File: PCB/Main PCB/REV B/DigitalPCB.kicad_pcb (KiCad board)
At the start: 4 copper layers, 60 x 80 mm, 102 parts, among them J1 DF12NC-20DS-0.5V_51_, J2 1050170001, J3 Hopper, J4 Screen, J5 Spare1, J6 Spare2, Q1 MBT3904DW1, U1 AMS1117-3.3, U2 ESP32-WROOM-32UE_16MB, U3 TPS2115APWR, U4 TLP2362TPR_E, U5 CP2102N-A02-GQFN24, U6 TLP2362TPR_E, U7 TLP2362TPR_E, U8 STM811SW16F

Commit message: PCB - digital routing underway
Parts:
- moved C12 1.10 mm to (101.8, 109.0)
- moved D2 1.10 mm to (98.0, 109.0)
- moved D6 1.10 mm to (100.8, 105.7)
- moved R2 1.10 mm to (99.9, 109.0)
- moved R27 0.30 mm to (95.9, 107.7)
- turned C1 to 0 degrees
- turned C7 to 90 degrees
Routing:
- net +3.3VA: track 0.00 -> 81.9 mm, vias 0 -> 9
- net +5VA: track 0.00 -> 20.3 mm
- net /IO13: track 0.00 -> 13.6 mm
- net /IO27: track 0.00 -> 13.2 mm
- net /IO26: track 0.00 -> 13.0 mm
- net /IO25: track 0.00 -> 12.8 mm
- net GND: track 0.00 -> 8.65 mm, vias 0 -> 52
- net +3.3V: track 0.00 -> 5.21 mm, vias 0 -> 19
- net Net-(JP1-Pad2): track 0.00 -> 4.62 mm
- net Net-(JP6-Pad2): track 0.00 -> 4.55 mm
- net Net-(JP2-Pad2): track 0.00 -> 4.26 mm
- net Net-(JP4-Pad2): track 0.00 -> 4.25 mm
- net Net-(D5-Pad2): track 0.00 -> 3.89 mm
- net Net-(D4-Pad2): track 0.00 -> 3.89 mm
- net Net-(D3-Pad2): track 0.00 -> 3.89 mm
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- added copper zone on F.Cu, net +3.3V
- added copper zone on In2.Cu, net +3.3V
- added copper zone on F.Cu, net +3.3VP
- added copper zone on B.Cu, net GND
- added copper zone on F.Cu, net GND
- added copper zone on In1.Cu, net GND

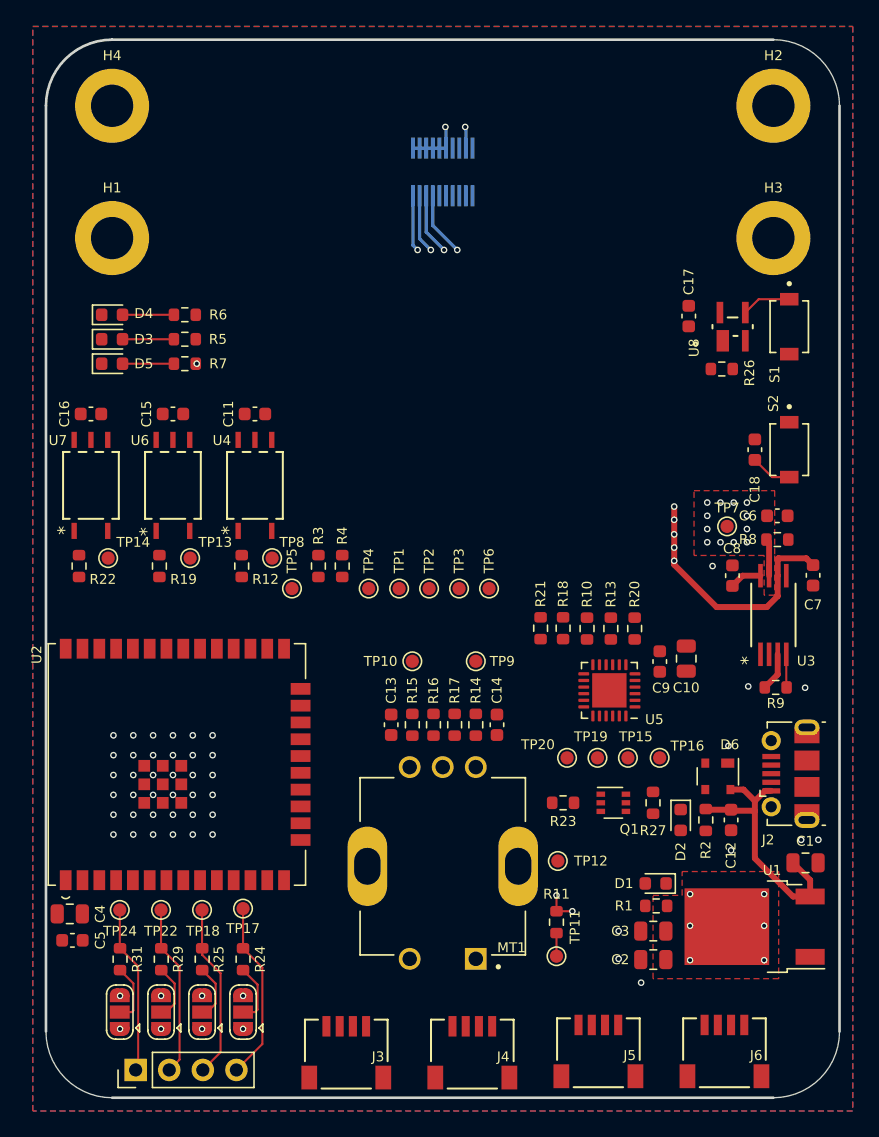
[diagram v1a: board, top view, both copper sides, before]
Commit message: PCB - digital routing halfway done
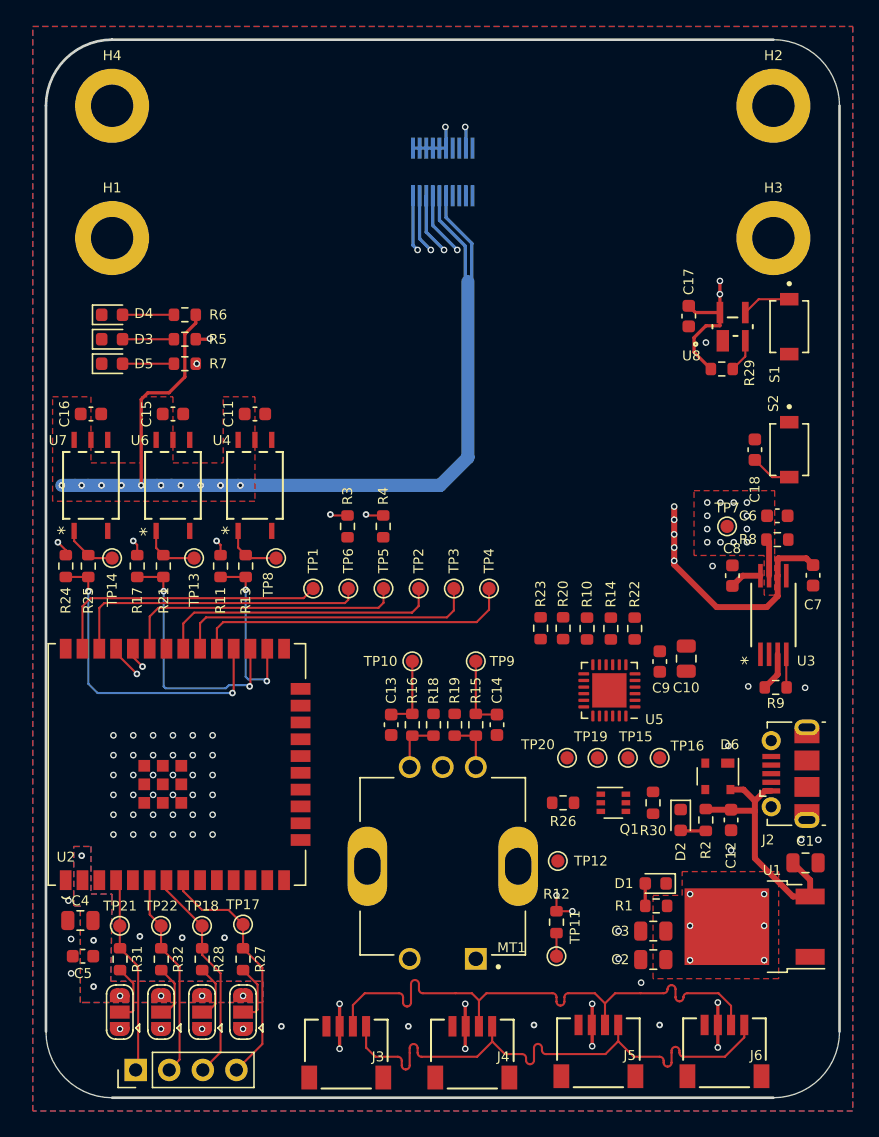
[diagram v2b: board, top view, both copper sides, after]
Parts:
- added R11: 10K 1% 0603, Resistor_SMD:R_0603_1608Metric, F.Cu at (63.2, 89.8)
- added R17: 10K 1% 0603, Resistor_SMD:R_0603_1608Metric, F.Cu at (56.9, 89.8)
- added R24: 10K 1% 0603, Resistor_SMD:R_0603_1608Metric, F.Cu at (51.5, 89.8)
- moved TP1 13.3 mm to (70.2, 91.5)
- moved R4 4.31 mm to (75.5, 86.8)
- moved TP6 4.26 mm to (72.9, 91.5)
- moved R3 3.72 mm to (72.8, 86.8)
- moved TP4 2.27 mm to (83.5, 91.5)
- moved TP3 1.87 mm to (80.8, 91.5)
- moved TP2 1.48 mm to (78.2, 91.5)
- moved C5 1.44 mm to (52.8, 119.3)
- moved TP17 1.20 mm to (64.9, 116.9)
- moved TP18 1.20 mm to (61.8, 117.0)
- moved TP21 1.20 mm to (55.6, 117.0)
- moved TP22 1.20 mm to (58.7, 117.0)
- moved TP5 1.12 mm to (75.5, 91.5)
- moved C4 0.94 mm to (52.6, 116.6)
- moved R25 0.70 mm to (53.2, 89.8)
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- renumbered JP6 to JP3, R11 to R12, R12 to R13, R13 to R14, R14 to R15, R15 to R16, R16 to R18, R17 to R19, R18 to R20, R19 to R21, R20 to R22, R21 to R23, R22 to R25, R23 to R26, R24 to R27, R25 to R28, R26 to R29, R27 to R30, R29 to R32, TP6 to TP1, TP1 to TP2, TP24 to TP21, TP26 to TP24, TP2 to TP3, TP3 to TP4, TP4 to TP5, TP5 to TP6
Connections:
- net /I39 renamed /IO39
- C13 pad 1: /IO32 -> /IO25
- C14 pad 1: /IO33 -> /IO26
- MT1 pad 2: /IO34 -> /IO33
- R12 pad 1: /IO34 -> /IO33
- R15 pad 2: /IO33 -> /IO26
- R16 pad 2: /IO32 -> /IO25
- R27 pad 1: /IO13 -> /IO32
- R28 pad 1: /IO27 -> /IO35
- R31 pad 1: /IO25 -> /IO36
- R32 pad 1: /IO26 -> /IO34
- TP10 pad 1: /IO32 -> /IO25
- TP11 pad 1: /IO34 -> /IO33
- TP17 pad 1: /IO13 -> /IO32
- TP18 pad 1: /IO27 -> /IO35
- TP21 pad 1: /IO25 -> /IO36
- TP22 pad 1: /IO26 -> /IO34
- TP24 pad 1: /IO25 -> /IO36
- TP24 pad 2: /IO26 -> /IO34
- TP24 pad 3: /IO27 -> /IO35
- TP24 pad 4: /IO13 -> /IO32
- TP9 pad 1: /IO33 -> /IO26
- U2 pad 23: /Auger -> /IO15
- U2 pad 26: /Fan -> /Auger
- U2 pad 27: /SPI_MOSI -> /Fan
- U2 pad 28: /IO17 -> /Ignitor
- U2 pad 37: /Ignitor -> /SPI_MOSI
- U2 pad 4: /I36 -> /IO36
- U2 pad 6: /I34 -> /IO34
- U2 pad 7: /I35 -> /IO35
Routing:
- net +5V: track 0.00 -> 75.2 mm, vias 0 -> 10
- net /I2C_SCL: track 0.00 -> 66.6 mm
- net /I2C_SDA: track 0.00 -> 64.8 mm
- net +3.3V: track 5.21 -> 36.1 mm, vias 19 -> 37
- net /Ignitor: track 0.00 -> 24.4 mm, vias 0 -> 2
- net /SPI_CS: track 0.00 -> 24.3 mm
- net /SPI_SCK: track 0.00 -> 23.2 mm
- net +3.3VA: track 81.9 -> 105.0 mm, vias 9 -> 10
- net /SPI_MISO: track 0.00 -> 21.6 mm
- net /SPI_MOSI: track 0.00 -> 21.2 mm
- net /Fan: track 0.00 -> 19.8 mm, vias 0 -> 2
- net /IO32: track 0.00 -> 18.8 mm
- net /TXD0: track 0.00 -> 17.3 mm, vias 0 -> 1
- net /IO35: track 0.00 -> 16.6 mm
- net /RXD0: track 0.00 -> 15.9 mm, vias 0 -> 1
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- added copper zone on B.Cu, net +3.3V
- added copper zone on F.Cu, net +5V

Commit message: PCB - digital routing first pass done
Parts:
- added C19: 0.1uF 50V X7R 0603, Capacitor_SMD:C_0603_1608Metric, F.Cu at (84.1, 78.0)
- added C20: 0.01uF 50V X7R 0603, Capacitor_SMD:C_0603_1608Metric, F.Cu at (86.8, 78.8)
- added U9: MAX31855KASA, Package_SO:SOIC-8_3.9x4.9mm_P1.27mm, F.Cu at (86.9, 83.6)
- moved TP16 7.31 mm to (94.0, 111.2)
- moved TP15 7.24 mm to (91.8, 111.2)
- moved R20 6.68 mm to (88.1, 101.1)
- moved R23 6.68 mm to (86.4, 101.1)
- moved TP20 4.63 mm to (88.9, 108.9)
- moved TP19 4.24 mm to (95.9, 104.9)
- moved D6 1.90 mm to (98.9, 105.7)
- moved R26 1.79 mm to (90.3, 106.4), turned to -90 degrees
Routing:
- net /EN: track 2.53 -> 96.3 mm, vias 0 -> 4
- net /MeatProbe-: track 0.00 -> 78.7 mm, vias 0 -> 1
- net /IO0: track 3.14 -> 80.3 mm, vias 0 -> 4
- net /MeatProbe+: track 0.00 -> 72.8 mm, vias 0 -> 1
- net /I2C_SDA: track 64.8 -> 120.1 mm, vias 0 -> 2
- net /I2C_SCL: track 66.6 -> 120.4 mm, vias 0 -> 2
- net /Opto_Fan: track 0.00 -> 51.9 mm, vias 0 -> 1
- net /Opto_Ignitor: track 0.00 -> 47.8 mm, vias 0 -> 1
- net +3.3VP: track 2.44 -> 38.6 mm, vias 6 -> 10
- net /Opto_Auger: track 0.00 -> 35.5 mm, vias 0 -> 1
- net +5V: track 75.2 -> 110.6 mm, vias 10 -> 14
- net /Probe1-: track 0.00 -> 32.9 mm, vias 0 -> 1
- net /IO33: track 1.75 -> 32.9 mm
- net /IO26: track 5.60 -> 35.3 mm
- net /IO25: track 5.60 -> 29.8 mm
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
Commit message: PCB - hopper pcb done routing ready for review
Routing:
- net GND: track 19.8 -> 18.5 mm, vias 84 -> 131
- net /IO36: track 15.1 -> 14.4 mm
- net /RXD0: track 36.7 -> 36.1 mm
- net +3.3VP: vias 10 -> 7

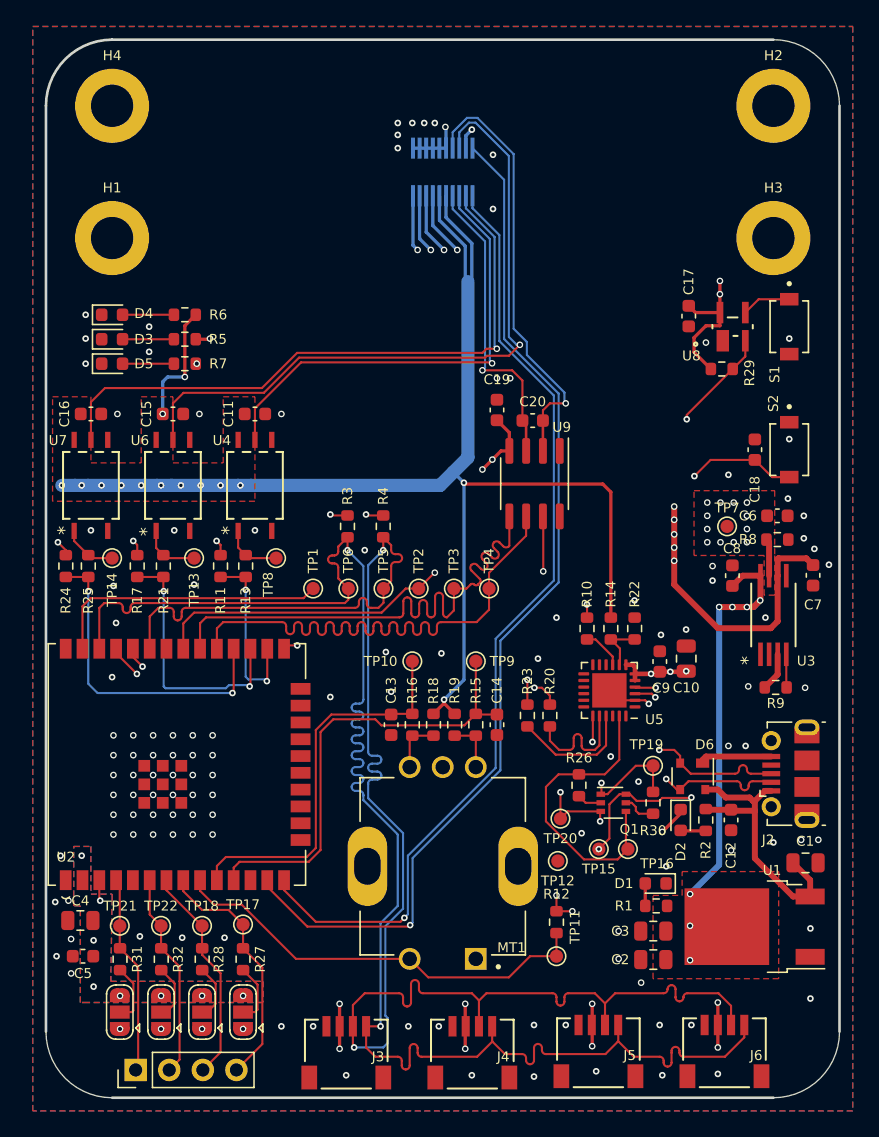
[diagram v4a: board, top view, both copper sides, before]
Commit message: PCB - Text edited, all ready for review
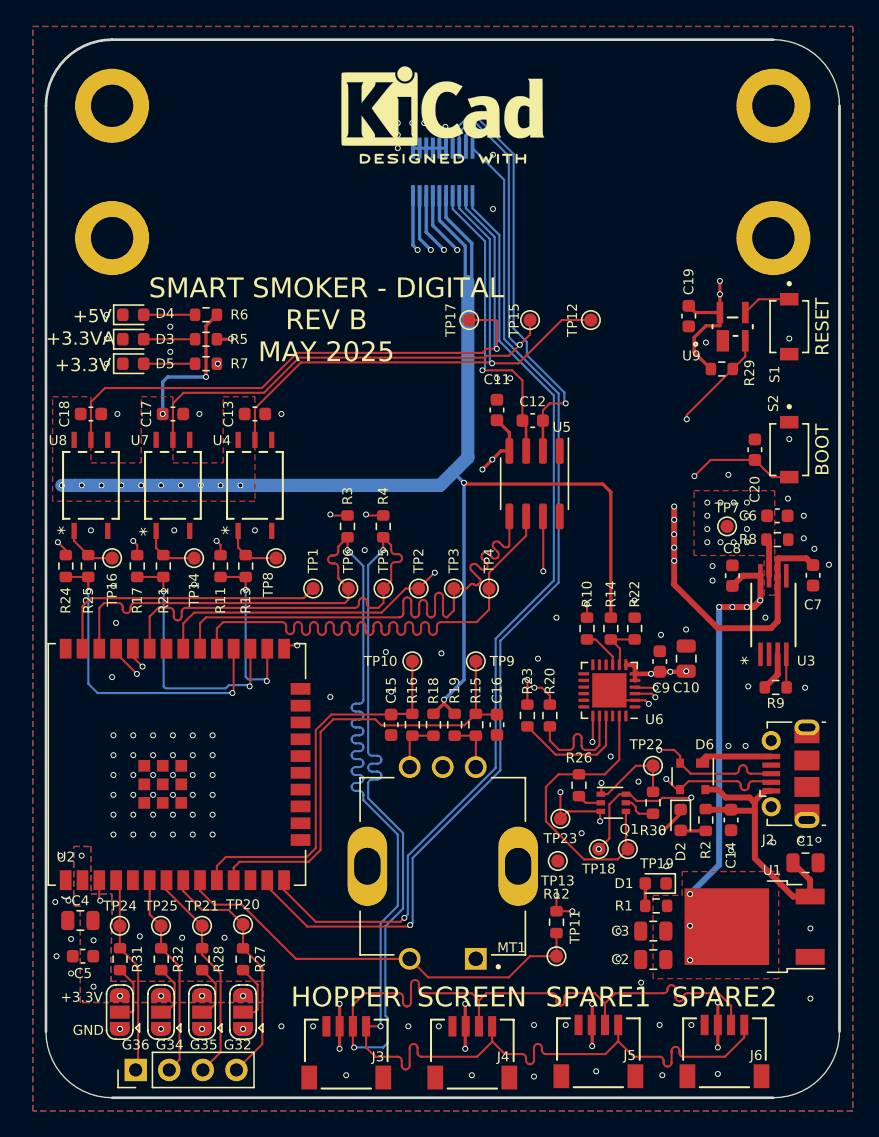
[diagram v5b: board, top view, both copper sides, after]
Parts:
- added REF**: KiCad-Logo2_6mm_SilkScreen, Symbol:KiCad-Logo2_6mm_SilkScreen, F.Cu at (80.0, 55.0)
- added TP12: TP, TestPoint:TestPoint_Pad_D1.0mm, F.Cu at (91.2, 71.2)
- added TP15: TP, TestPoint:TestPoint_Pad_D1.0mm, F.Cu at (86.6, 71.2)
- added TP17: TP, TestPoint:TestPoint_Pad_D1.0mm, F.Cu at (82.0, 71.2)
- moved D3 1.60 mm to (56.6, 72.7)
- moved D4 1.60 mm to (56.6, 70.8)
- moved D5 1.60 mm to (56.6, 74.5)
- moved R5 1.60 mm to (62.1, 72.7)
- moved R6 1.60 mm to (62.1, 70.8)
- moved R7 1.60 mm to (62.1, 74.5)
- renumbered C19 to C11, C20 to C12, C11 to C13, C12 to C14, C13 to C15, C14 to C16, C15 to C17, C16 to C18, C17 to C19, C18 to C20, TP12 to TP13, TP13 to TP14, TP14 to TP16, TP15 to TP18, TP16 to TP19, TP17 to TP20, TP18 to TP21, TP19 to TP22, TP20 to TP23, TP21 to TP24, TP22 to TP25, TP24 to TP27, U9 to U5, U5 to U6, U6 to U7, U7 to U8, U8 to U9
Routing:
- net /Opto_Auger: track 35.5 -> 44.3 mm
- net /Opto_Ignitor: track 47.8 -> 52.0 mm
- net /Opto_Fan: track 51.9 -> 54.1 mm
- net +3.3VA: track 108.3 -> 106.7 mm
- net +5V: track 110.6 -> 112.2 mm
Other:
- board text added: "+3.3V"
- board text added: "+3.3VA"
- board text added: "+5V"
- board text added: "BOOT"
- board text added: "DIM: 80mm X 60mm HOLE: 10mm x 50mm x 3mm"
- board text added: "G32"
- board text added: "G34"
- board text added: "G35"
- board text added: "G36"
- board text added: "GND"
- board text added: "HOPPER"
- board text added: "RESET"
- board text added: "SCREEN"
- board text added: "SMART SMOKER - DIGITAL REV B MAY 2025"
- board text added: "SPARE1"
- board text added: "SPARE2"

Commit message: PCB - gerbers generated and boms started
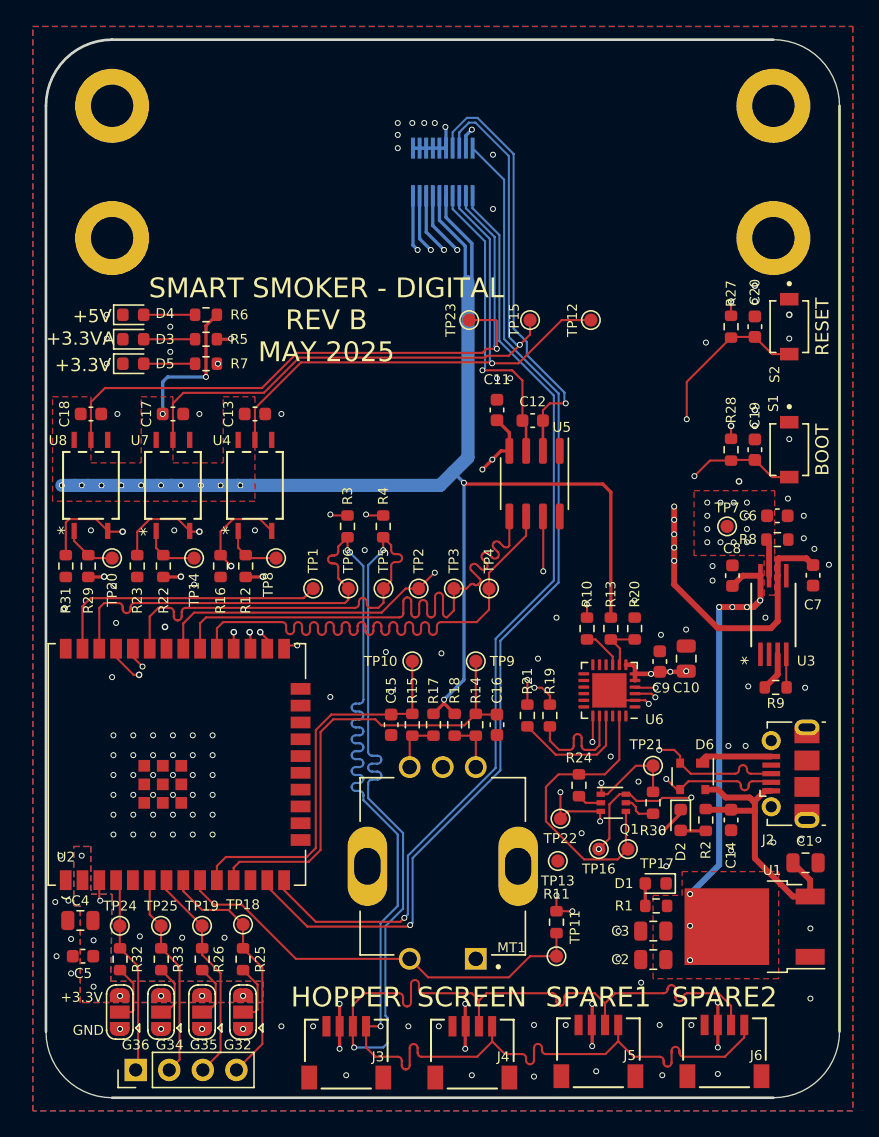
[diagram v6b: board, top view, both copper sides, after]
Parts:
- removed REF**: KiCad-Logo2_6mm_SilkScreen, Symbol:KiCad-Logo2_6mm_SilkScreen
- removed U9: STM811SW16F, Customs Smoker:STM811SW16F
- added R28: 10K 1% 0603, Resistor_SMD:R_0603_1608Metric, F.Cu at (101.8, 81.0)
- R12: renamed from R13; value 140Ohm 1% 0603 -> 150Ohm 1% 0603
- R22: renamed from R21; value 140Ohm 1% 0603 -> 150Ohm 1% 0603
- R29: renamed from R25; value 140Ohm 1% 0603 -> 150Ohm 1% 0603
- moved C20 5.06 mm to (103.6, 71.7)
- moved R27 3.28 mm to (101.8, 71.7), turned to 90 degrees
- renumbered C20 to C19, C19 to C20, R12 to R11, R14 to R13, R15 to R14, R16 to R15, R11 to R16, R18 to R17, R19 to R18, R20 to R19, R22 to R20, R23 to R21, R17 to R23, R26 to R24, R27 to R25, R28 to R26, R29 to R27, R24 to R31, R31 to R32, R32 to R33, S2 to S1, S1 to S2, TP18 to TP16, TP19 to TP17, TP20 to TP18, TP21 to TP19, TP16 to TP20, TP22 to TP21, TP23 to TP22, TP17 to TP23
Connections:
- C20 pad 1: GND -> /EN
- C20 pad 2: +3.3V -> GND
- R12 pad 1: /Auger -> +3.3V
- R16 pad 1: +3.3V -> /Auger
- R16 pad 2: /Auger -> GND
- R22 pad 1: /Fan -> +3.3V
- R23 pad 1: +3.3V -> /Fan
- R23 pad 2: /Fan -> GND
- R29 pad 1: /Ignitor -> +3.3V
- R31 pad 1: +3.3V -> /Ignitor
- R31 pad 2: /Ignitor -> GND
- S2 pad 1: Net-(S1-Pad1) -> GND
- S2 pad 2: GND -> /EN
- U4 pad 3: GND -> /Auger
- U7 pad 3: GND -> /Fan
- U8 pad 3: GND -> /Ignitor
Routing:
- net +3.3V: track 47.7 -> 38.8 mm
- net /EN: track 96.3 -> 101.0 mm
- net Net-(S1-Pad1): track 3.74 -> 0.00 mm
- net /Auger: track 13.6 -> 14.9 mm
- net /Fan: track 19.8 -> 18.7 mm
- net /Ignitor: track 24.4 -> 23.7 mm
- net GND: vias 131 -> 138
